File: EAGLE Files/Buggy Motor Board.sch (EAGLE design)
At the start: 21 parts, among them IC1 ILD213T, IC2 ILD213T, IC3 74HC595D

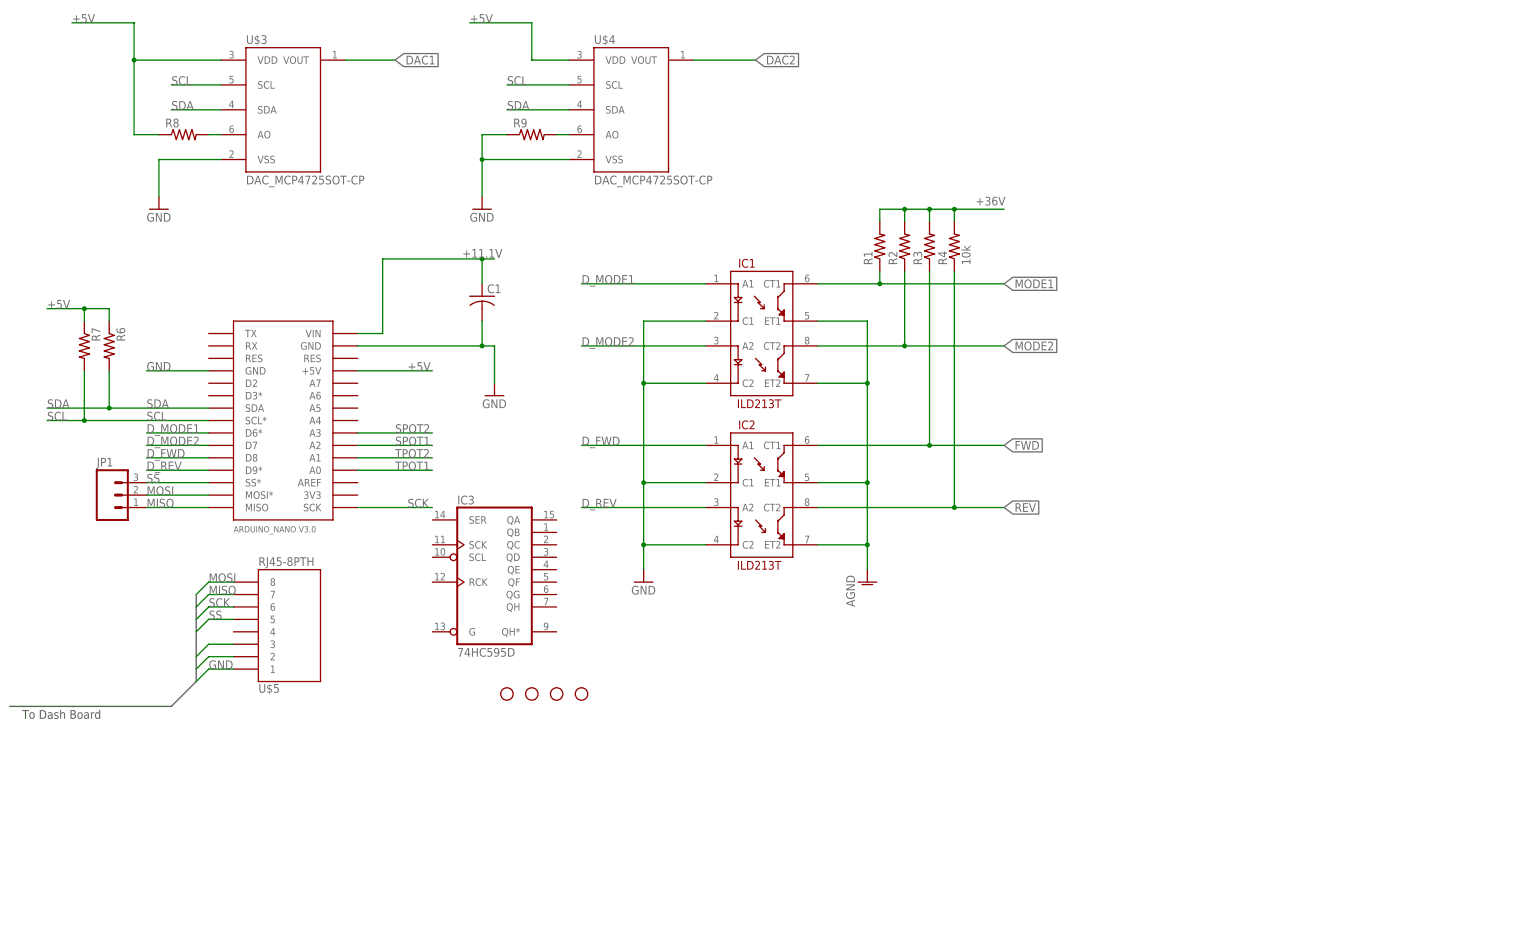
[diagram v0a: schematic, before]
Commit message: Add CAN support to schematic, high side drivers.
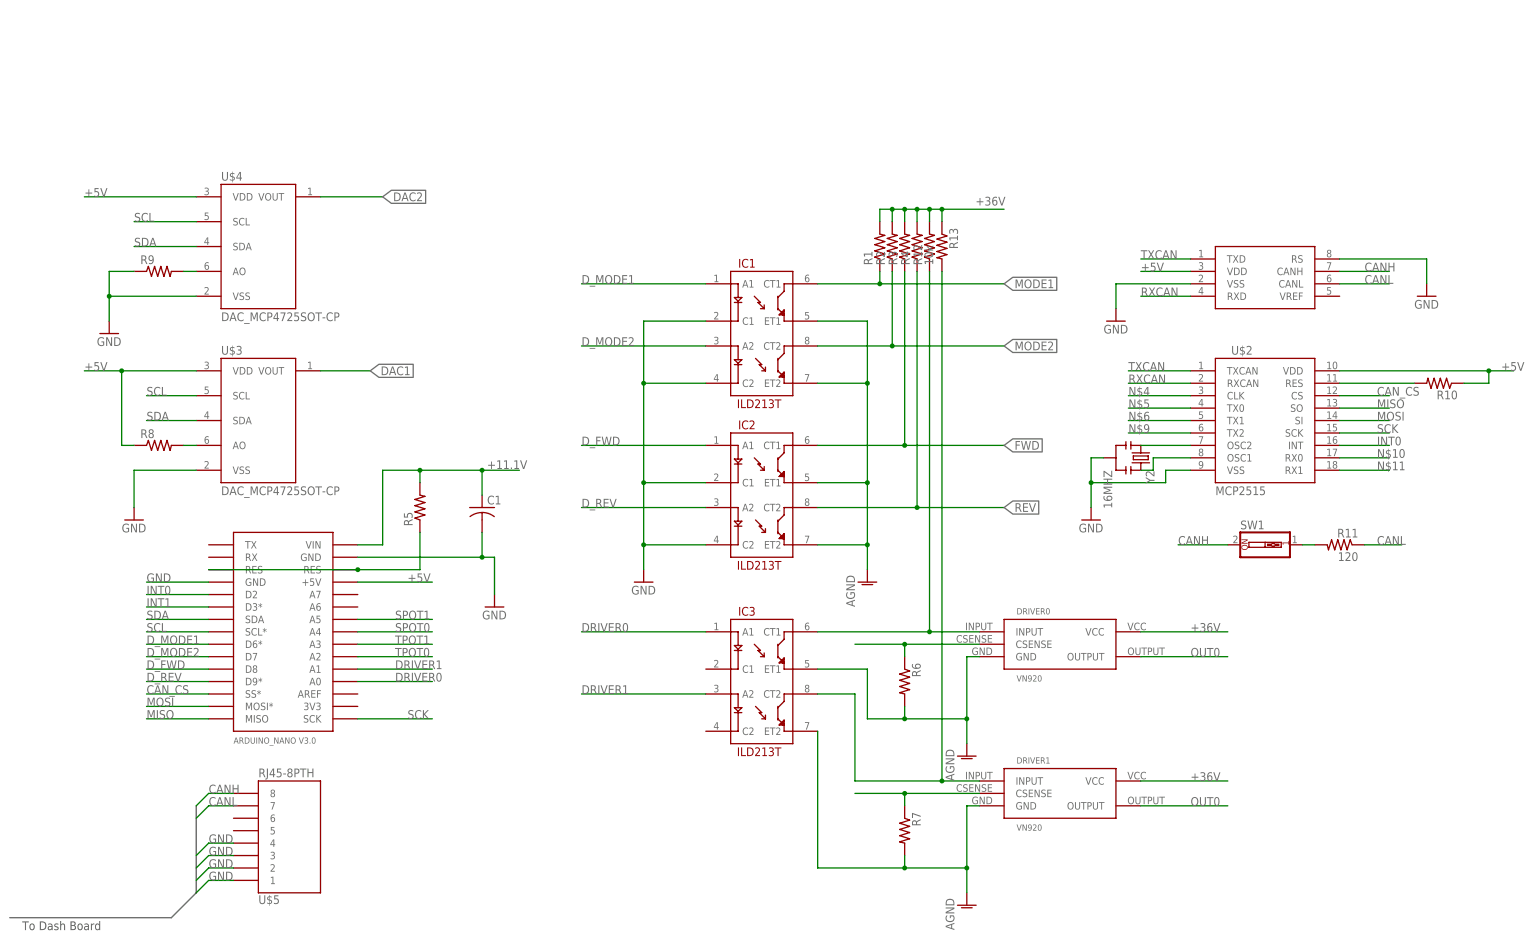
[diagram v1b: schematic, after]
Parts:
- removed JP1: (no value), SparkFun-Connectors:M03SCREW
- removed STANDOFF1, STANDOFF2, STANDOFF3, STANDOFF4: STAND-OFF, SparkFun-Electromechanical:STAND-OFF
- added DRIVER0, DRIVER1: VN920, Wetmelon-DiscreteSemi:VN920
- added R10, R12, R13, R5: (no value), rcl:R-US_R1206
- added R11: 120, rcl:R-US_R1206
- added SW1: (no value), special:SW_DIP-1
- added U$2: MCP2515, Wetmelon-DigitalIC:MCP2515
- added U1: MCP2551, SparkFun-DigitalIC:MCP2551
- added Y2: 16MHZ, SparkFun-FreqCtrl:RESONATOR16MHZ
- IC3: value 74HC595D -> ILD213T; device 74xx-eu:74HC595D -> SparkFun-DiscreteSemi:ILD213T
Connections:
- removed net SPOT2: U$1.A3
- removed net SS: JP1.3, U$1.SS*, U$5.5
- removed net TPOT2: U$1.A1
- new net CANH: SW1.2, U$5.8, U1.CANH
- new net CANL: R11.1, U$5.7, U1.CANL
- new net CAN_CS: U$1.SS*, U$2.CS
- new net DRIVER0: IC3.A1, U$1.A0
- new net DRIVER1: IC3.A2, U$1.A1
- new net INT0: U$1.D2, U$2.INT
- new net INT1: U$1.D3*
- new net N$1: DRIVER0.INPUT, IC3.CT1, R12.1
- new net N$10: U$2.RX0
- new net N$11: U$2.RX1
- new net N$12: DRIVER0.CSENSE, R6.1
- new net N$13: R11.2, SW1.1
- new net N$14: U$2.OSC2, Y2.1
- new net N$15: DRIVER1.CSENSE, R7.1
- new net N$16: DRIVER1.INPUT, IC3.CT2, R13.2
- new net N$2: U$2.OSC1, Y2.3
- new net N$3: R10.2, U$2.RES
- new net N$4: U$2.CLK
- new net N$5: U$2.TX0
- new net N$6: U$2.TX1
- new net N$9: U$2.TX2
- new net OUT0: DRIVER0.OUTPUT, DRIVER1.OUTPUT
- new net RES: R5.1, U$1.RES, U$1.RES@1
- new net RXCAN: U$2.RXCAN, U1.RXD
- new net SPOT0: U$1.A4
- new net TPOT0: U$1.A2
- new net TXCAN: U$2.TXCAN, U1.TXD
- net +11.1V: now also R5.2
- net +36V: now also DRIVER0.VCC, DRIVER1.VCC, R12.2, R13.1
- net +5V: now also R10.1, U$2.VDD, U1.VDD; no longer R6.1, R7.1
- net AGND: now also DRIVER0.GND, DRIVER1.GND, IC3.ET1, IC3.ET2, R6.2, R7.2
- net GND: now also U$2.VSS, U$5.2, U$5.3, U$5.4, U1.RS, U1.VSS, Y2.2
- net MISO: now also U$2.SO; no longer JP1.1, U$5.7
- net MOSI: now also U$2.SI; no longer JP1.2, U$5.8
- net SCK: now also U$2.SCK; no longer U$5.6
- net SCL: no longer R7.2, U$5.3
- net SDA: no longer R6.2, U$5.2
- net SPOT1: now also U$1.A5; no longer U$1.A2
- net TPOT1: now also U$1.A3; no longer U$1.A0
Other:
- moved on the sheet: C1, R2, R3, R4, R6, R7, R8, R9, U$3, U$4, U$5

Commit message: Add SD Card slot & level shifter
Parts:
- added ACT: RED, adafruit:LEDCHIP-LED0805
- added C2: 10uF/10V, adafruit:CPOL-USA/3216-18R
- added C3: 0.1uF, adafruit:C-USC0805K
- added IC4: 4050D, 40xx:4050D
- added IC5: LP298XS, adafruit:LP298XS
- added JP1: (no value), adafruit:PINHD-1X8BIG
- added R14: 1K, adafruit:R-US_R0805
- added U$6, U$7: FIDUCIAL, adafruit:FIDUCIAL
- added X1: MICROSD, adafruit:MICROSD
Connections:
- new net +3V3: C2.+, IC4P.VDD, IC5.VOUT, JP1.2, U$1.3V3, X1.VDD
- new net CD: JP1.8, X1.CARD_DETECT
- new net CLK: IC4A.I, IC4D.I, JP1.4
- new net CS: IC4C.I, JP1.7
- new net DI: IC4B.I, JP1.6
- new net DO: JP1.5, X1.DATA_OUT
- new net N$17: ACT.A, IC4D.O
- new net N$18: IC4A.O, X1.SCLK
- new net N$19: IC4C.O, R14.1, X1.CS
- new net N$20: ACT.C, R14.2
- new net N$21: IC4B.O, X1.DATA_IN
- net +5V: now also C3.1, IC5.EN, IC5.VIN, JP1.1
- net GND: now also C2.-, C3.2, IC4E.I, IC4F.I, IC4P.VSS, IC5.GND, JP1.3, X1.GND, X1.GND1, X1.VSS

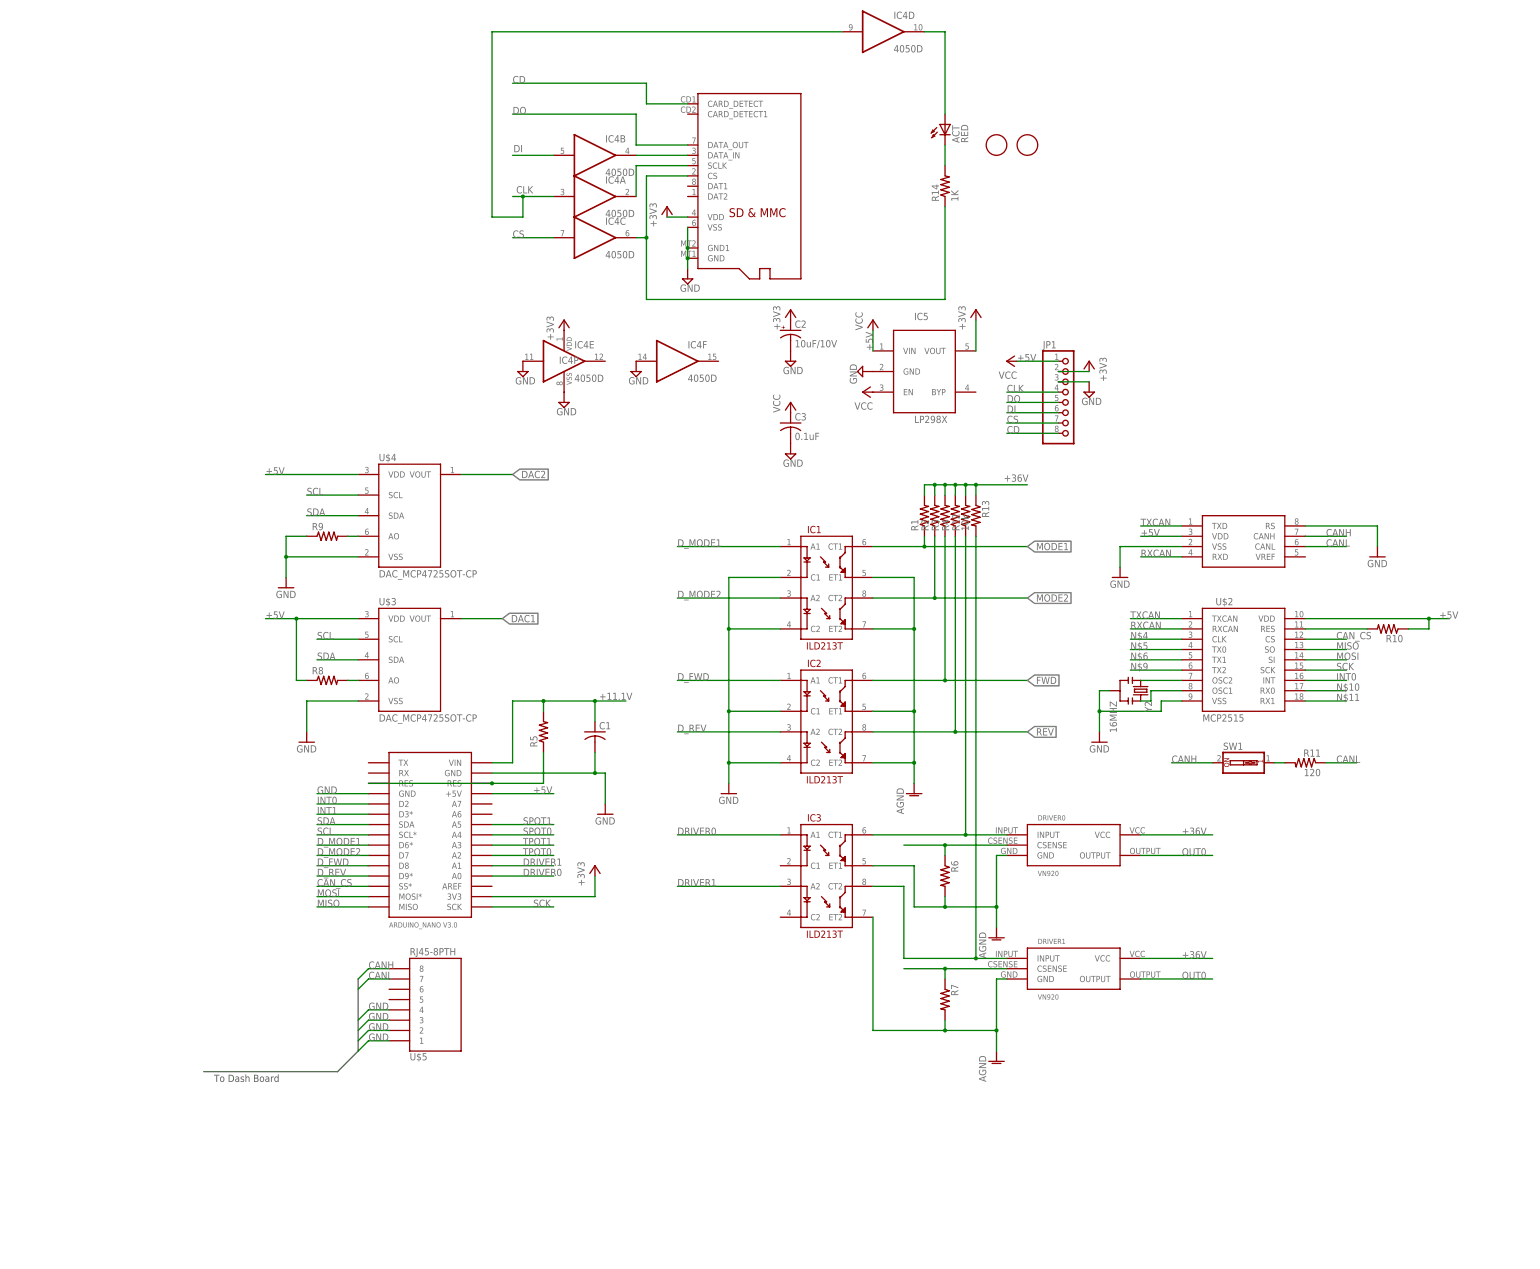
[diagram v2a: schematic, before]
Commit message: Add analog multiplexer, shift register
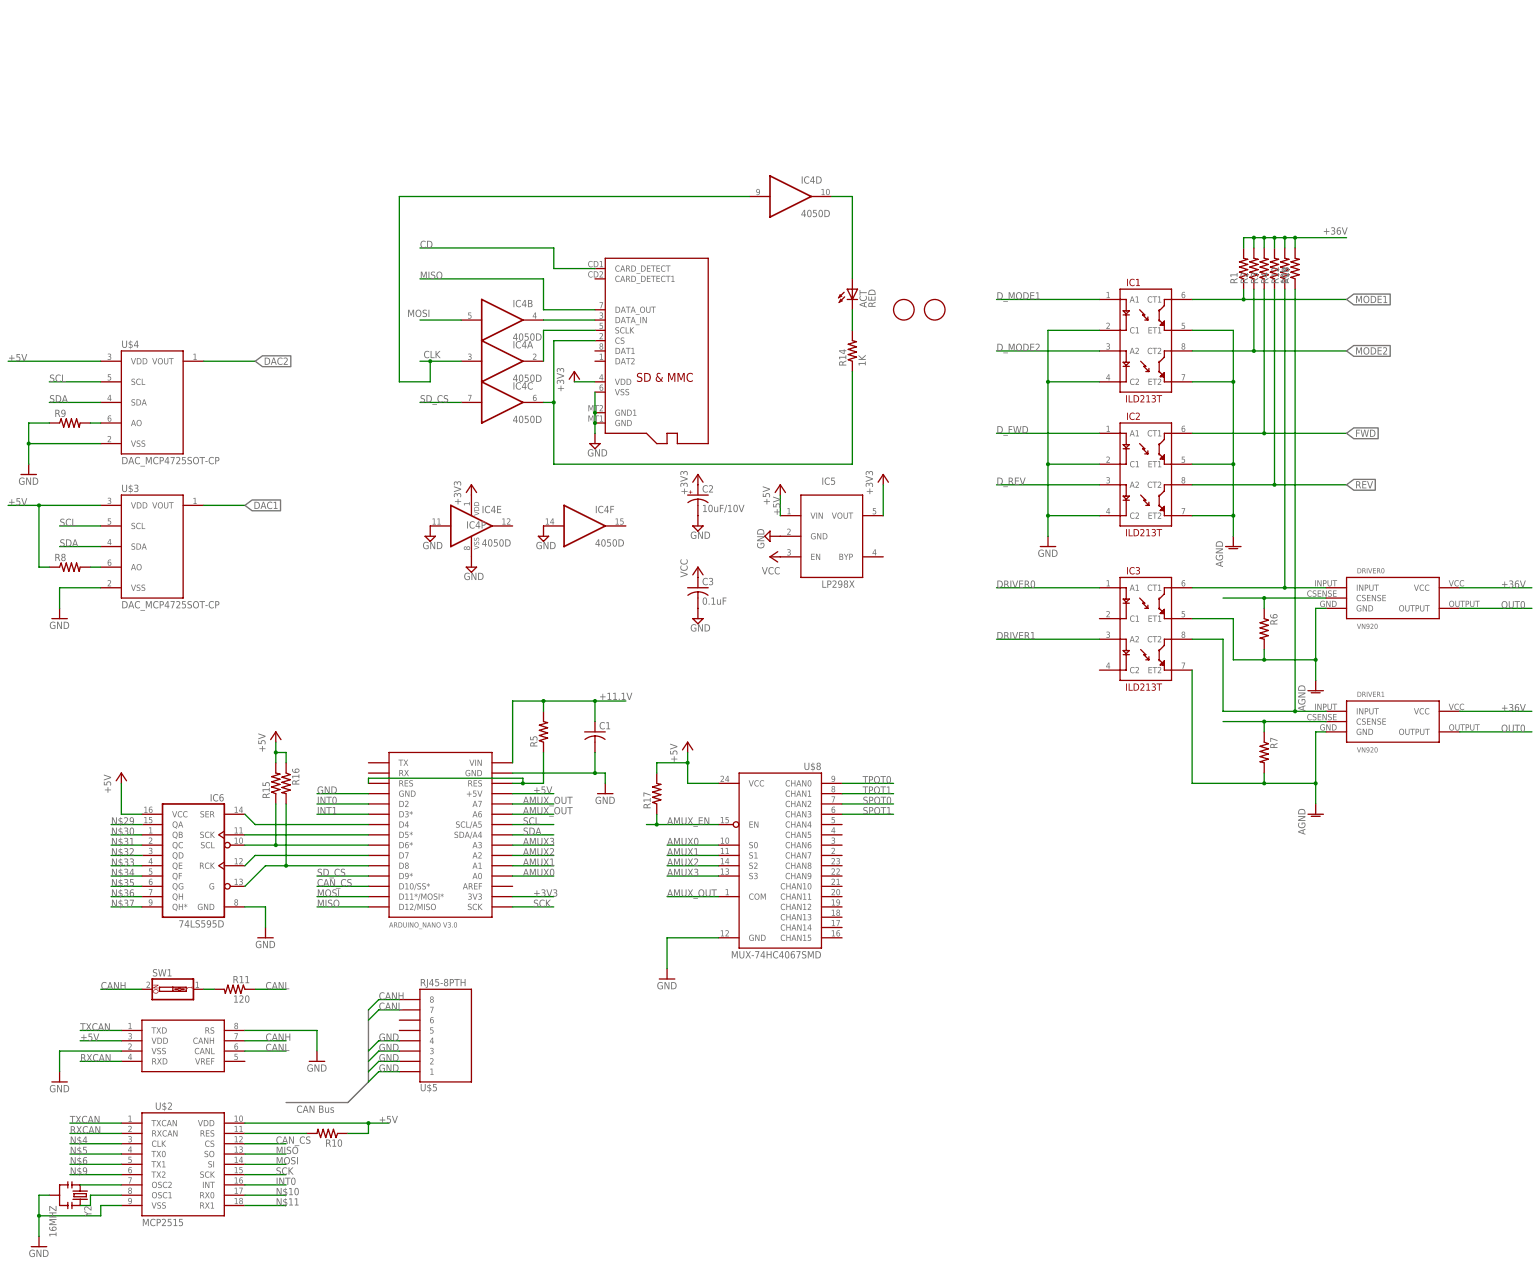
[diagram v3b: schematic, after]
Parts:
- removed JP1: (no value), adafruit:PINHD-1X8BIG
- added IC6: 74LS595D, SparkFun-DigitalIC:74LS595D
- added R15, R16, R17: (no value), rcl:R-US_R1206
- added U$8: MUX-74HC4067SMD, SparkFun-AnalogIC:MUX-74HC4067SMD
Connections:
- net RES renamed N$23
- removed net CS: IC4C.I, JP1.7
- removed net DI: IC4B.I, JP1.6
- removed net DO: JP1.5, X1.DATA_OUT
- new net AMUX0: U$1.A0, U$8.S0
- new net AMUX1: U$1.A1, U$8.S1
- new net AMUX2: U$1.A2, U$8.S2
- new net AMUX3: U$1.A3, U$8.S3
- new net AMUX_EN: R17.1, U$8.EN
- new net AMUX_OUT: U$1.A6, U$1.A7, U$8.COM
- new net N$22: IC6.SCL, R15.1, U$1.D6*
- new net N$24: IC6.SER, U$1.D4
- new net N$25: IC6.SCK, U$1.D5*
- new net N$26: IC6.RCK, U$1.D7
- new net N$28: IC6.G, R16.2, U$1.D8
- new net N$29: IC6.QA
- new net N$30: IC6.QB
- new net N$31: IC6.QC
- new net N$32: IC6.QD
- new net N$33: IC6.QE
- new net N$34: IC6.QF
- new net N$35: IC6.QG
- new net N$36: IC6.QH
- new net N$37: IC6.QH*
- new net SD_CS: IC4C.I, U$1.D9*
- net +36V: now also R13.2; no longer R13.1
- net +3V3: no longer JP1.2
- net +5V: now also IC6.VCC, R15.2, R16.1, R17.2, U$8.VCC; no longer JP1.1
- net CAN_CS: now also U$1.D10/SS*; no longer U$1.SS*
- net CD: no longer JP1.8
- net CLK: no longer JP1.4
- net DRIVER0: no longer U$1.A0
- net DRIVER1: no longer U$1.A1
- net D_FWD: no longer U$1.D8
- net D_MODE1: no longer U$1.D6*
- net D_MODE2: no longer U$1.D7
- net D_REV: no longer U$1.D9*
- net GND: now also IC6.GND, U$8.GND; no longer JP1.3
- net MISO: now also U$1.D12/MISO, X1.DATA_OUT; no longer U$1.MISO
- net MOSI: now also IC4B.I, U$1.D11*/MOSI*; no longer U$1.MOSI*
- net N$16: now also R13.1; no longer R13.2
- net SCL: now also U$1.SCL/A5; no longer U$1.SCL*
- net SDA: now also U$1.SDA/A4; no longer U$1.SDA
- net SPOT0: now also U$8.CHAN2; no longer U$1.A4
- net SPOT1: now also U$8.CHAN3; no longer U$1.A5
- net TPOT0: now also U$8.CHAN0; no longer U$1.A2
- net TPOT1: now also U$8.CHAN1; no longer U$1.A3
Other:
- note added: "CAN Bus"
- note removed: "To Dash Board"
- moved on the sheet: ACT, C2, C3, DRIVER0, DRIVER1, IC1, IC2, IC3, IC4A, IC4B, IC4C, IC4D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
